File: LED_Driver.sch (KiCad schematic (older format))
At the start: 0 parts

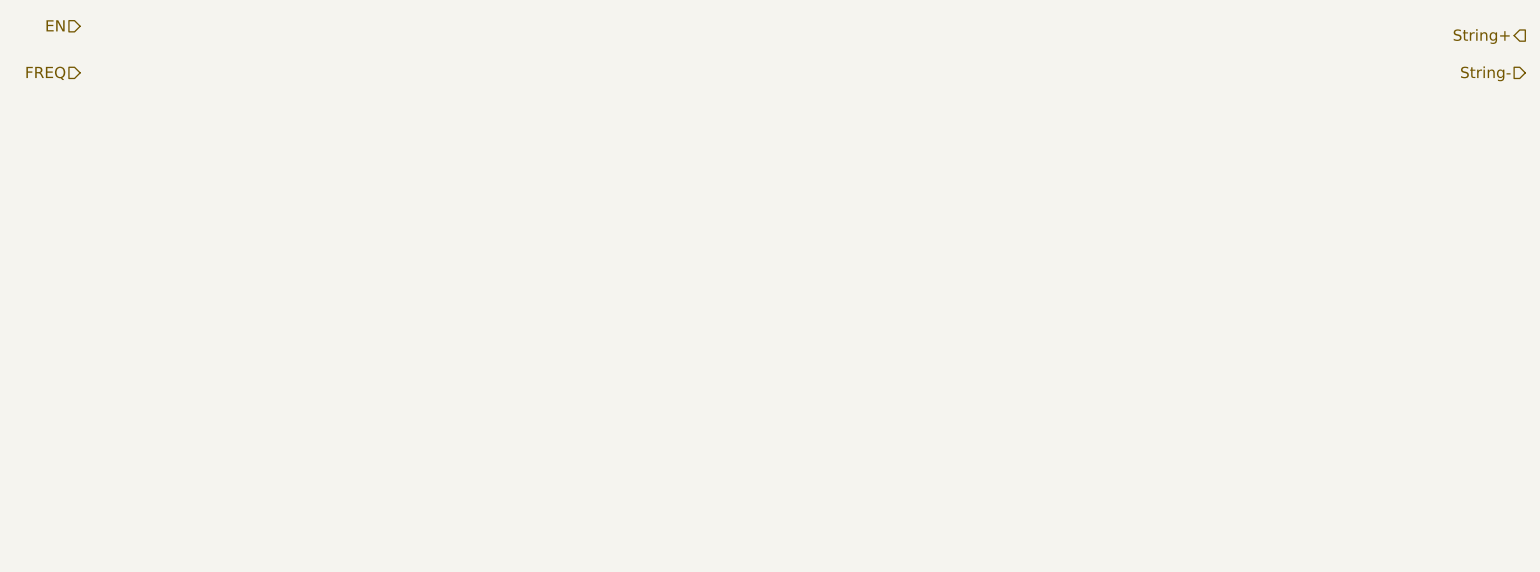
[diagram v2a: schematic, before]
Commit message: Completed LED Driver Video + Power Module
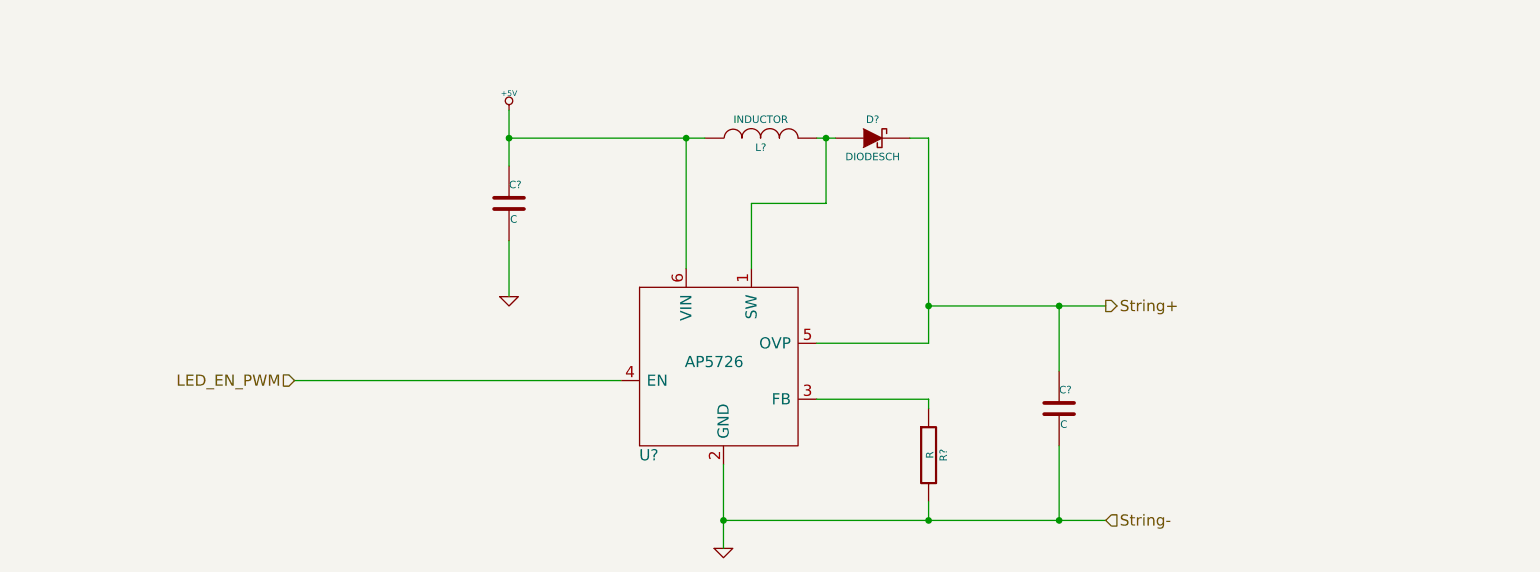
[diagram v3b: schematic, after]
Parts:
- added C? (x2): C, ~, symbol C
- added D?: DIODESCH, ~, symbol DIODESCH
- added L?: INDUCTOR, ~, symbol INDUCTOR
- added R?: R, ~, symbol R
- added U?: AP5726, symbol AP5726
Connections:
- net String+: now also C?.1, D?.2 (K), U?.5 (OVP)
- new net: D?.1 (A), L?.2, U?.1 (SW)
- new net: R?.1, U?.3 (FB)
- new net +5V: C?.1, L?.1, U?.6 (VIN)
- new net GND: C?.2, C?.2, R?.2, U?.2 (GND)
- new net LED_EN_PWM: U?.4 (EN)
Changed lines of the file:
@@
 LIBS:contrib
 LIBS:valves
+LIBS:BenchBudEE_Parts
 LIBS:BenchBudEE-cache
 EELAYER 27 0
@@
 $Descr A4 11693 8268
 encoding utf-8
-Sheet 6 8
+Sheet 5 9
 Title ""
-Date "6 feb 2014"
+Date "10 feb 2014"
 Rev ""
 Comp ""
@@
 Comment4 ""
 $EndDescr
-Text HLabel 1950 2050 0    60   Input ~ 0
-EN
-Text HLabel 1950 2300 0    60   Input ~ 0
-FREQ
-Text HLabel 9700 2100 0    60   Output ~ 0
+Text HLabel 3100 3950 0    60   Input ~ 0
+LED_EN_PWM
+Text HLabel 7450 3550 2    60   Output ~ 0
 String+
-Text HLabel 9700 2300 0    60   Input ~ 0
+Text HLabel 7450 4700 2    60   Input ~ 0
 String-
+$Comp
+L AP5726 U?
+U 1 1 52F869ED
+P 5350 3950
+F 0 "U?" H 5000 3550 60  0000 C CNN
+F 1 "AP5726" H 5350 4050 60  0000 C CNN
+F 2 "" H 5350 3950 60  0000 C CNN
+F 3 "" H 5350 3950 60  0000 C CNN
+	1    5350 3950
+	1    0    0    -1
+$EndComp
+Wire Wire Line
+	4850 3950 3100 3950
+$Comp
+L +5V #PWR?
+U 1 1 52F8746B
+P 4250 2500
+F 0 "#PWR?" H 4250 2590 20  0001 C CNN
+F 1 "+5V" H 4250 2590 30  0000 C CNN
+F 2 "" H 4250 2500 60  0000 C CNN
+F 3 "" H 4250 2500 60  0000 C CNN
+	1    4250 2500
+	1    0    0    -1
+$EndComp
+$Comp
+L GND #PWR?
+U 1 1 52F8747A
+P 4250 3500
+F 0 "#PWR?" H 4250 3500 30  0001 C CNN
+F 1 "GND" H 4250 3430 30  0001 C CNN
+F 2 "" H 4250 3500 60  0000 C CNN
+F 3 "" H 4250 3500 60  0000 C CNN
+	1    4250 3500
+	1    0    0    -1
+$EndComp
+$Comp
+L C C?
+U 1 1 52F87493
+P 4250 3000
+F 0 "C?" H 4250 3100 40  0000 L CNN
+F 1 "C" H 4256 2915 40  0000 L CNN
+F 2 "~" H 4288 2850 30  0000 C CNN
+F 3 "~" H 4250 3000 60  0000 C CNN
+	1    4250 3000
+	1    0    0    -1
+$EndComp
+$Comp
+L GND #PWR?
+U 1 1 52F874B4
+P 5400 4850
+F 0 "#PWR?" H 5400 4850 30  0001 C CNN
+F 1 "GND" H 5400 4780 30  0001 C CNN
+F 2 "" H 5400 4850 60  0000 C CNN
+F 3 "" H 5400 4850 60  0000 C CNN
+	1    5400 4850
+	1    0    0    -1
+$EndComp
+Wire Wire Line
+	5400 4400 5400 4850
+$Comp
+L R R?
+U 1 1 52F874BE
+P 6500 4350
+F 0 "R?" V 6580 4350 40  0000 C CNN
+F 1 "R" V 6507 4351 40  0000 C CNN
+F 2 "~" V 6430 4350 30  0000 C CNN
+F 3 "~" H 6500 4350 30  0000 C CNN
+	1    6500 4350
+	1    0    0    -1
+$EndComp
+Wire Wire Line
+	4250 2500 4250 2800
+Wire Wire Line
+	4250 3200 4250 3500
+Wire Wire Line
+	4250 2650 5300 2650
+Connection ~ 4250 2650
+Wire Wire Line
+	5200 2650 5200 3350
+$Comp
+L INDUCTOR L?
+U 1 1 52F874E8
+P 5600 2650
+F 0 "L?" V 5550 2650 40  0000 C CNN
+F 1 "INDUCTOR" V 5700 2650 40  0000 C CNN
+F 2 "~" H 5600 2650 60  0000 C CNN
+F 3 "~" H 5600 2650 60  0000 C CNN
+	1    5600 2650
+	0    -1   -1   0
+$EndComp
+Connection ~ 5200 2650
+Wire Wire Line
+	5550 3350 5550 3000
+Wire Wire Line
+	5550 3000 5950 3000
+Wire Wire Line
+	5950 3000 5950 2650
+Wire Wire Line
+	5900 2650 6000 2650
+$Comp
+L DIODESCH D?
+U 1 1 52F87514
+P 6200 2650
+F 0 "D?" H 6200 2750 40  0000 C CNN
+F 1 "DIODESCH" H 6200 2550 40  0000 C CNN
+F 2 "~" H 6200 2650 60  0000 C CNN
+F 3 "~" H 6200 2650 60  0000 C CNN
+	1    6200 2650
+	1    0    0    -1
+$EndComp
+Connection ~ 5950 2650
+Wire Wire Line
+	6500 2650 6500 3750
+Wire Wire Line
+	6500 2650 6400 2650
+Wire Wire Line
+	6500 4100 6500 4050
+Wire Wire Line
+	6500 4600 6500 4700
+Wire Wire Line
+	5400 4700 7450 4700
+Connection ~ 5400 4700
+$Comp
+L C C?
+U 1 1 52F875A6
+P 7200 4100
+F 0 "C?" H 7200 4200 40  0000 L CNN
+F 1 "C" H 7206 4015 40  0000 L CNN
+F 2 "~" H 7238 3950 30  0000 C CNN
+F 3 "~" H 7200 4100 60  0000 C CNN
+	1    7200 4100
+	1    0    0    -1
+$EndComp
+Wire Wire Line
+	6500 3750 5900 3750
+Wire Wire Line
+	6500 3550 7450 3550
+Connection ~ 6500 3550
+Connection ~ 6500 4700
+Wire Wire Line
+	6500 4050 5900 4050
+Wire Wire Line
+	7200 4300 7200 4700
+Connection ~ 7200 4700
+Wire Wire Line
+	7200 3550 7200 3900
+Connection ~ 7200 3550
 $EndSCHEMATC

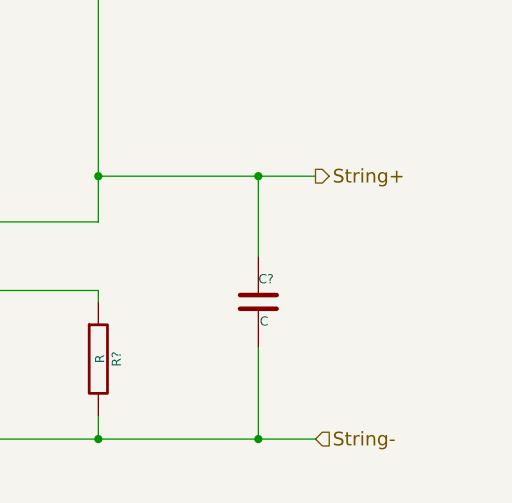
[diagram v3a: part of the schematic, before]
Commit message: Completed Arduino Module Video
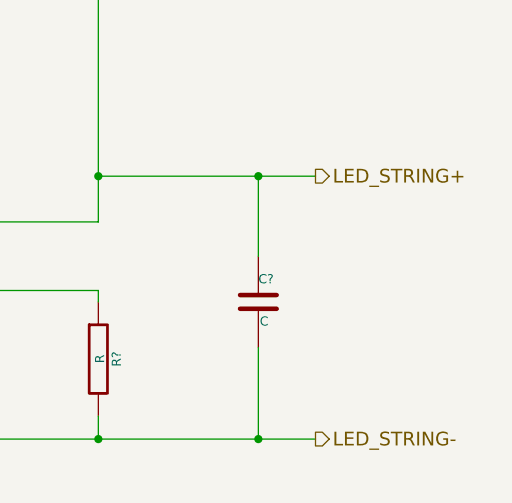
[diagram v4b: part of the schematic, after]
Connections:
- net String+ renamed LED_STRING+
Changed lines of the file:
@@
 Sheet 5 9
 Title ""
-Date "10 feb 2014"
+Date "11 feb 2014"
 Rev ""
 Comp ""
@@
 LED_EN_PWM
 Text HLabel 7450 3550 2    60   Output ~ 0
-String+
-Text HLabel 7450 4700 2    60   Input ~ 0
-String-
+LED_STRING+
+Text HLabel 7450 4700 2    60   Output ~ 0
+LED_STRING-
 $Comp
 L AP5726 U?

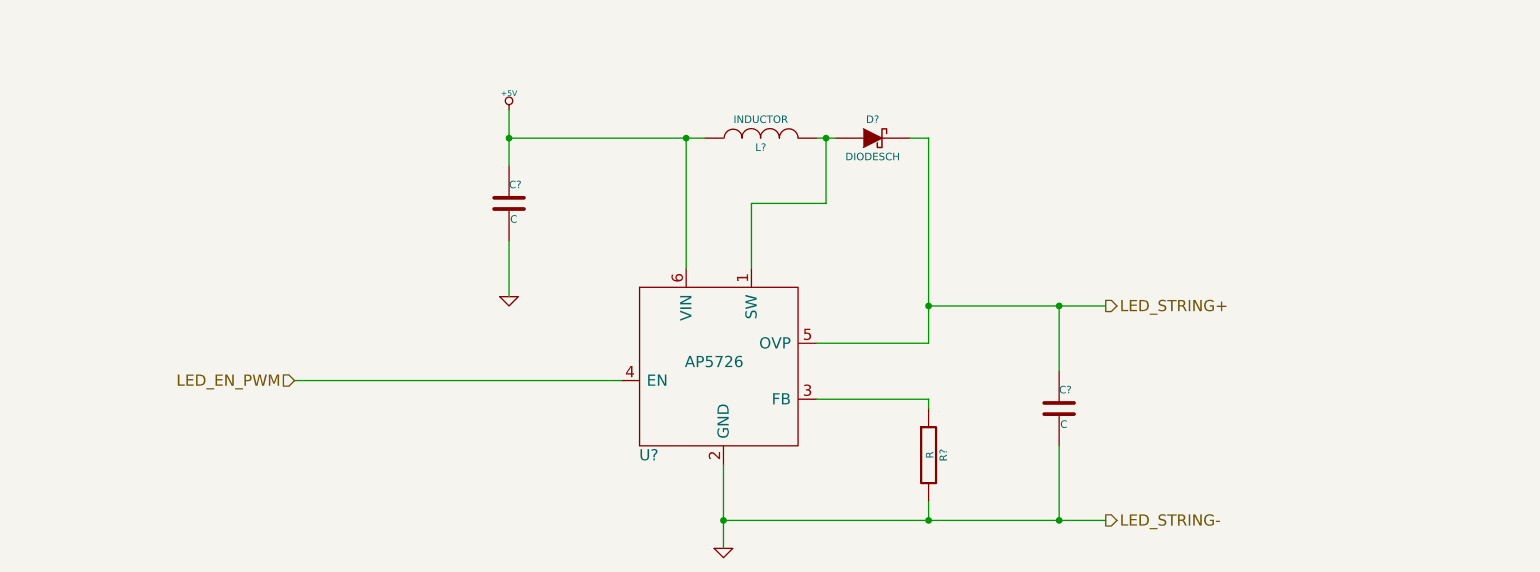
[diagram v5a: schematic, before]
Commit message: started associating relay parts
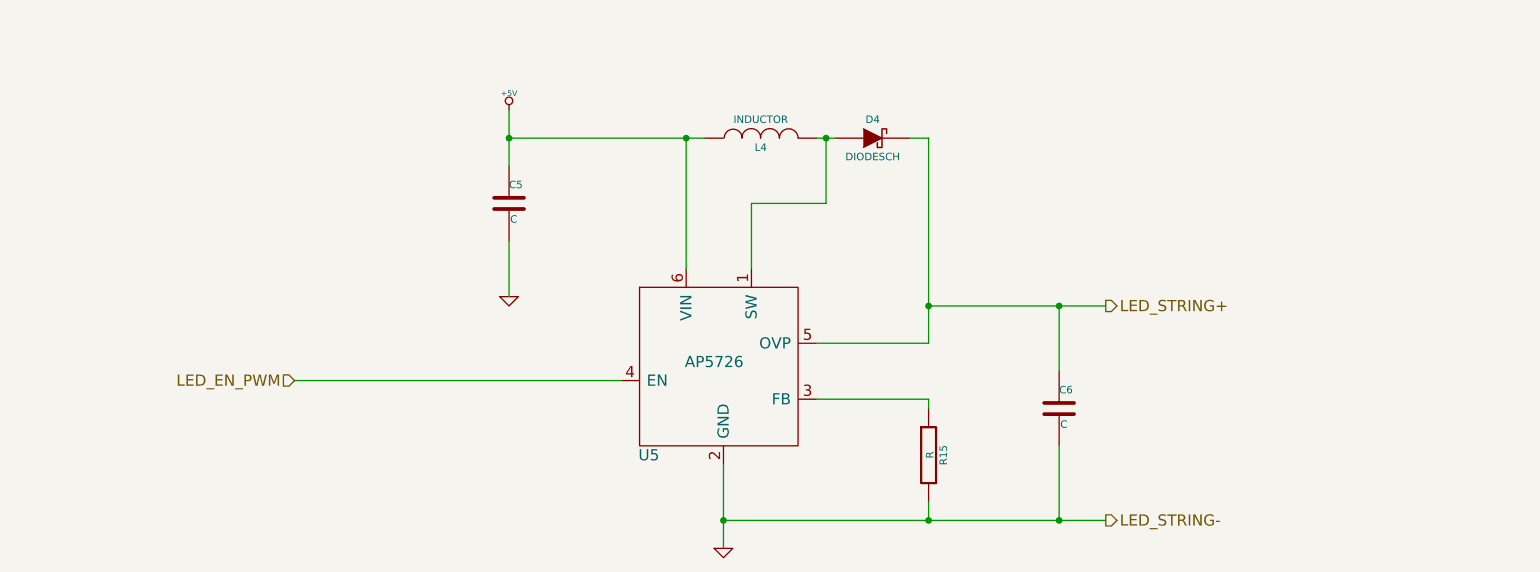
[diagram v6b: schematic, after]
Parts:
- gave numbers to parts that had none: 6
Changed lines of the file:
@@
 Sheet 5 9
 Title ""
-Date "17 feb 2014"
+Date "20 feb 2014"
 Rev ""
 Comp ""
@@
 LED_STRING-
 $Comp
-L AP5726 U?
+L AP5726 U5
 U 1 1 52F869ED
 P 5350 3950
-F 0 "U?" H 5000 3550 60  0000 C CNN
+F 0 "U5" H 5000 3550 60  0000 C CNN
 F 1 "AP5726" H 5350 4050 60  0000 C CNN
 F 2 "" H 5350 3950 60  0000 C CNN
@@
 	4850 3950 3100 3950
 $Comp
-L +5V #PWR?
+L +5V #PWR024
 U 1 1 52F8746B
 P 4250 2500
-F 0 "#PWR?" H 4250 2590 20  0001 C CNN
+F 0 "#PWR024" H 4250 2590 20  0001 C CNN
 F 1 "+5V" H 4250 2590 30  0000 C CNN
 F 2 "" H 4250 2500 60  0000 C CNN
@@
 $EndComp
 $Comp
-L GND #PWR?
+L GND #PWR025
 U 1 1 52F8747A
 P 4250 3500
-F 0 "#PWR?" H 4250 3500 30  0001 C CNN
+F 0 "#PWR025" H 4250 3500 30  0001 C CNN
 F 1 "GND" H 4250 3430 30  0001 C CNN
 F 2 "" H 4250 3500 60  0000 C CNN
@@
 $EndComp
 $Comp
-L C C?
+L C C5
 U 1 1 52F87493
 P 4250 3000
-F 0 "C?" H 4250 3100 40  0000 L CNN
+F 0 "C5" H 4250 3100 40  0000 L CNN
 F 1 "C" H 4256 2915 40  0000 L CNN
 F 2 "~" H 4288 2850 30  0000 C CNN
@@
 $EndComp
 $Comp
-L GND #PWR?
+L GND #PWR026
 U 1 1 52F874B4
 P 5400 4850
-F 0 "#PWR?" H 5400 4850 30  0001 C CNN
+F 0 "#PWR026" H 5400 4850 30  0001 C CNN
 F 1 "GND" H 5400 4780 30  0001 C CNN
 F 2 "" H 5400 4850 60  0000 C CNN
@@
 	5400 4400 5400 4850
 $Comp
-L R R?
+L R R15
 U 1 1 52F874BE
 P 6500 4350
-F 0 "R?" V 6580 4350 40  0000 C CNN
+F 0 "R15" V 6580 4350 40  0000 C CNN
 F 1 "R" V 6507 4351 40  0000 C CNN
 F 2 "~" V 6430 4350 30  0000 C CNN
@@
 	5200 2650 5200 3350
 $Comp
-L INDUCTOR L?
+L INDUCTOR L4
 U 1 1 52F874E8
 P 5600 2650
-F 0 "L?" V 5550 2650 40  0000 C CNN
+F 0 "L4" V 5550 2650 40  0000 C CNN
 F 1 "INDUCTOR" V 5700 2650 40  0000 C CNN
 F 2 "~" H 5600 2650 60  0000 C CNN
@@
 	5900 2650 6000 2650
 $Comp
-L DIODESCH D?
+L DIODESCH D4
 U 1 1 52F87514
 P 6200 2650
-F 0 "D?" H 6200 2750 40  0000 C CNN
+F 0 "D4" H 6200 2750 40  0000 C CNN
 F 1 "DIODESCH" H 6200 2550 40  0000 C CNN
 F 2 "~" H 6200 2650 60  0000 C CNN
@@
 Connection ~ 5400 4700
 $Comp
-L C C?
+L C C6
 U 1 1 52F875A6
 P 7200 4100
-F 0 "C?" H 7200 4200 40  0000 L CNN
+F 0 "C6" H 7200 4200 40  0000 L CNN
 F 1 "C" H 7206 4015 40  0000 L CNN
 F 2 "~" H 7238 3950 30  0000 C CNN
